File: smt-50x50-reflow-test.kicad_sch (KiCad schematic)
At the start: 0 parts

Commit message: schem: import esp32-c6, uart, usb-c, flash, crystal, buttons, tmp117, bmp581 from esp32c6-sensor-devboard
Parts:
- added AE1: Antenna, RF_Antenna:Johanson_2450AT18x100, symbol Device:Antenna
- added C10, C11, C16, C17, C18, C48, C49, C50, C51: 0u1, Capacitor_SMD:C_0402_1005Metric, symbol Device:C
- added C13: 10n, Capacitor_SMD:C_0402_1005Metric, symbol Device:C
- added C14, C15, C19, C9: 1u, Capacitor_SMD:C_0402_1005Metric, symbol Device:C
- added C20, C8: 10u, Capacitor_SMD:C_0402_1005Metric, symbol Device:C
- added C23, C25: 12p, Capacitor_SMD:C_0402_1005Metric, symbol Device:C
- added C28, C29: 1p2, Capacitor_SMD:C_0402_1005Metric, symbol Device:C
- added C52: 1p, Capacitor_SMD:C_0402_1005Metric, symbol Device:C
- added D7: D_Schottky, Diode_SMD:D_SMA, symbol Device:D_Schottky
- added J1, J8: Conn_01x04_Pin, Connector_PinHeader_2.54mm:PinHeader_1x04_P2.54mm_Vertical, symbol Connector:Conn_01x04_Pin
- added J4: USB_C_Receptacle_USB2.0_14P, Connector_USB:USB_C_Receptacle_HRO_TYPE-C-31-M-12, symbol Connector:USB_C_Receptacle_USB2.0_14P
- added J9: Conn_01x03_Pin, Connector_PinHeader_2.54mm:PinHeader_1x03_P2.54mm_Vertical, symbol Connector:Conn_01x03_Pin
- added L2, L4, L7: 2n7, Inductor_SMD:L_0402_1005Metric, symbol Device:L
- added L3: 24n, Inductor_SMD:L_0402_1005Metric, symbol Device:L
- added L6: 3n9, Inductor_SMD:L_0402_1005Metric, symbol Device:L
- added R1, R2, R3, R4, R5, R6: 0, Resistor_SMD:R_0402_1005Metric, symbol Device:R
- added R10, R14: 22, Resistor_SMD:R_0402_1005Metric, symbol Device:R
- added R12, R13: 5k1, Resistor_SMD:R_0603_1608Metric, symbol Device:R
- added R16: 470, Resistor_SMD:R_0402_1005Metric, symbol Device:R
- added R57, R58, R62, R9: 10k, Resistor_SMD:R_0603_1608Metric, symbol Device:R
- added R7, R8: 10k, symbol Device:R
- added SW1, SW2: SW_Push, Button_Switch_SMD:SW_SPST_TS-1088-xR020, symbol Switch:SW_Push
- added U1: ESP32-C6, Package_DFN_QFN:QFN-40-1EP_5x5mm_P0.4mm_EP3.6x3.6mm_ThermalVias, symbol PCM_Espressif:ESP32-C6
- added U14, U16: TMP117AIDRV, Package_SON:WSON-6-1EP_2x2mm_P0.65mm_EP1x1.6mm, symbol Sensor_Temperature:TMP117xxDRV
- added U15: BMP581, Pers:Bosch_LGA-10_2x2mm_P0.8mm_AntiClockwisePinNumbering, symbol Pers:BMP581
- added U2: W25Q128JVS, Package_SO:SOIC-8_5.3x5.3mm_P1.27mm, symbol Memory_Flash:W25Q128JVS
- added U7: USBLC6-2SC6, Package_TO_SOT_SMD:SOT-23-6, symbol Power_Protection:USBLC6-2SC6
- added Y1: 48M, Crystal:Crystal_SMD_2016-4Pin_2.0x1.6mm, symbol Device:Crystal_GND24
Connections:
- new net: J4.A5 (CC1), R12.2
- new net: J4.A6 (D+), J4.B6 (D+), U7.3 (I/O2)
- new net: J4.A7 (D-), J4.B7 (D-), U7.1 (I/O1)
- new net: J4.B5 (CC2), R13.2
- new net: R2.1, U2.2 (DO/IO_{1})
- new net: R2.2, U1.21 (SPIQ/GPIO25)
- new net: C52.2, L6.2, L7.2
- new net: R5.1, U2.6 (CLK)
- new net: R5.2, U1.25 (SPICLK/GPIO29)
- new net: R58.1, U15.5 (SDO)
- new net: C11.1, L2.2, U1.2 (VDDA3P3), U1.3 (VDDA3P3)
- new net: R1.1, U2.1 (~{CS})
- new net: R3.1, U2.3 (~{WP}/IO_{2})
- new net: R6.1, U2.5 (DI/IO_{0})
- new net: R4.1, U2.7 (~{HOLD}/~{RESET}/IO_{3})
- new net: C15.1, C16.1, U1.23 (VDD_SPI/GPIO27), U2.8 (VCC)
- new net: R1.2, U1.20 (SPICS0/GPIO24)
- new net: J8.1 (Pin_1), U1.10 (MTMS/GPIO4/FSPIHD/ADC1_CH4)
- new net: J8.2 (Pin_2), U1.11 (MTDI/GPIO5/FSPIWP/ADC1_CH5)
- new net: J8.3 (Pin_3), U1.12 (MTCK/GPIO6/FSPICLK/ADC1_CH6)
- new net: J8.4 (Pin_4), U1.13 (MTDO/GPIO7/FSPID)
- new net: R4.2, U1.24 (SPIHD/GPIO28)
- new net: R3.2, U1.22 (SPIWP/GPIO26)
- new net: R6.2, U1.26 (SPID/GPIO30)
- new net: J1.4 (Pin_4), R16.1
- new net: R8.2, U1.15 (GPIO9)
- new net: R7.2, U1.14 (GPIO8)
- new net +3V3: C10.1, C13.1, C14.1, C17.1, C18.1, C48.1, C49.2, C50.1, C51.1, C8.1, C9.1, J1.1 (Pin_1), L2.1, R57.1, R58.2, R62.1, R7.1, R8.1, R9.2, U1.28 (VDDPST2), U1.37 (VDDA1), U1.40 (VDDA2), U1.5 (VDDPST1), U14.5 (V+), U15.1 (VDDIO), U15.10 (VDD), U15.6 (CSB), U16.4 (ADD0), U16.5 (V+)
- new net +5V: C20.1, D7.1 (K)
- new net BMP_INT1: U15.7 (INT)
- new net BOOT/SCL: SW1.2, U14.1 (SCL), U15.2 (SCK), U16.1 (SCL)
- new net CHIP_PU: C19.1, R9.1, SW2.2, U1.4 (CHIP_PU)
- new net D+: R10.2, U7.4 (I/O2)
- new net D-: R14.2, U7.6 (I/O1)
- new net ESP_D+: R10.1, U1.19 (GPIO13/USB_D+)
- new net ESP_D-: R14.1, U1.18 (GPIO12/USB_D-)
- new net GND: C10.2, C11.2, C13.2, C14.2, C15.2, C16.2, C17.2, C18.2, C19.2, C20.2, C23.1, C25.2, C28.2, C29.2, C48.2, C49.1, C50.2, C51.2, C8.2, C9.2, J1.3 (Pin_3), J4.A1 (GND), J4.A12 (GND), J4.B1 (GND), J4.B12 (GND), J4.S1 (SHIELD), J9.1 (Pin_1), J9.2 (Pin_2), J9.3 (Pin_3), L7.1, R12.1, R13.1, SW1.1, SW2.1, U1.41 (GND), U14.2 (GND), U14.4 (ADD0), U15.3 (GND), U15.8 (GND), U15.9 (GND), U16.2 (GND), U2.4 (GND), U7.2 (GND), Y1.2, Y1.4
- new net RF_ANT: AE1.1 (A), L6.1
- new net RF_ESP: C28.1, L4.2, U1.1 (ANT)
- new net RF_TRANS: C29.1, C52.1, L4.1
- new net SDA: U14.6 (SDA), U15.4 (SDI), U16.6 (SDA)
- new net TMP117_ALERT: R57.2, U14.3 (ALERT)
- new net TMP117_ALERT2: R62.2, U16.3 (ALERT)
- new net U0RXD: J1.2 (Pin_2), U1.30 (U0RXD/GPIO17/FSPICS1)
- new net U0TXD: R16.2, U1.29 (U0TXD/GPIO16/FSPICS0)
- new net VBUS: D7.2 (A), J4.A4 (VBUS), J4.A9 (VBUS), J4.B4 (VBUS), J4.B9 (VBUS), U7.5 (VBUS)
- new net XTAL_32K_N: U1.7 (GPIO1/XTAL_32K_N/ADC1_CH1)
- new net XTAL_32K_P: U1.6 (GPIO0/XTAL_32K_P/ADC1_CH0)
- new net XTAL_N: C25.1, U1.38 (XTAL_N), Y1.3
- new net XTAL_P: L3.1, U1.39 (XTAL_P)
- new net XTAL_PL: C23.2, L3.2, Y1.1
- no-connect marks 0 -> 3
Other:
- note added: "BMP581 I2C"
- note added: "Buttons"
- note added: "EN RC delay"
- note added: "HSE"
- note added: "Power"
- note added: "QFlash"
- note added: "TMP117 Temperature 1"
- note added: "TMP117 Temperature 2"
- note added: "UART"
- note added: "USB/ESP"

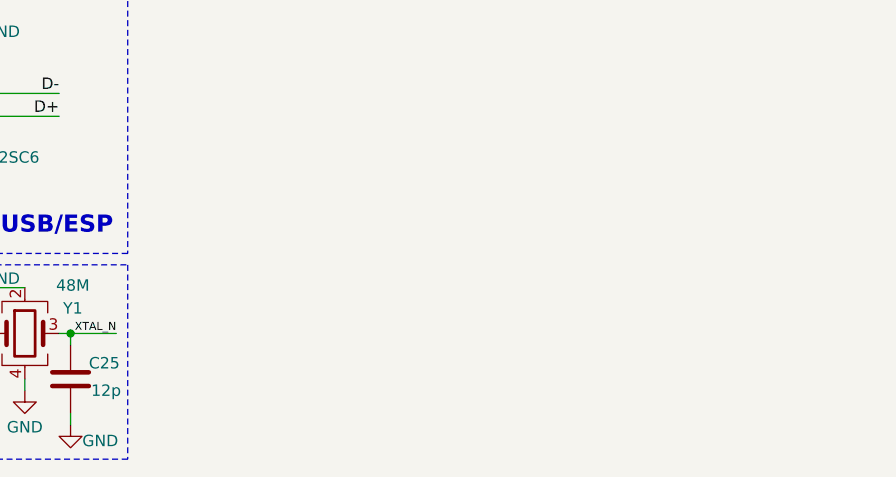
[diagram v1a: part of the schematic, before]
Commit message: schem: add LM317A 3v3 ldo
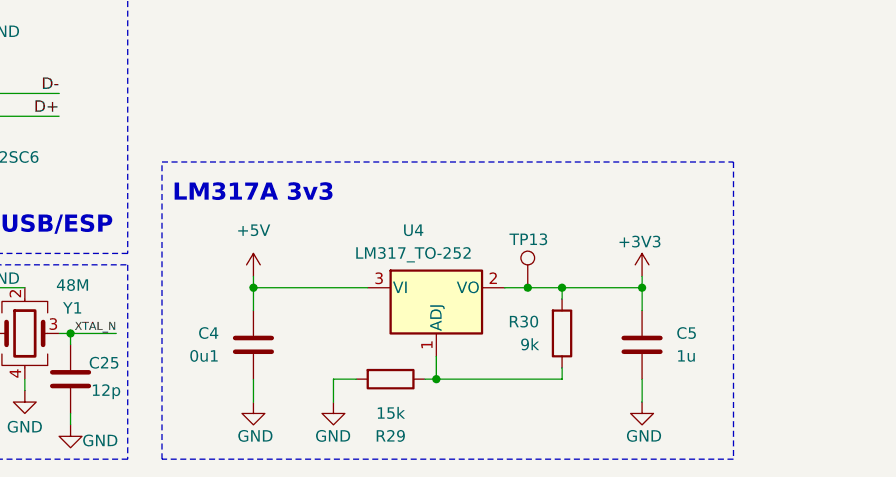
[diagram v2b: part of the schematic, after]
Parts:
- added C4: 0u1, Capacitor_SMD:C_0603_1608Metric, symbol Device:C
- added C5: 1u, Capacitor_SMD:C_0603_1608Metric, symbol Device:C
- added R29: 15k, Resistor_SMD:R_0603_1608Metric, symbol Device:R
- added R30: 9k, Resistor_SMD:R_0603_1608Metric, symbol Device:R
- added TP13: TestPoint, TestPoint:TestPoint_Pad_D2.0mm, symbol Connector:TestPoint
- added U4: LM317_TO-252, Package_TO_SOT_SMD:TO-252-2, symbol Regulator_Linear:LM317_TO-252
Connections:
- net +3V3: now also C5.1, R30.2, TP13.1, U4.2 (VO)
- net +5V: now also C4.1, U4.3 (VI)
- net GND: now also C4.2, C5.2, R29.2
- new net: R29.1, R30.1, U4.1 (ADJ)
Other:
- note added: "LM317A 3v3"

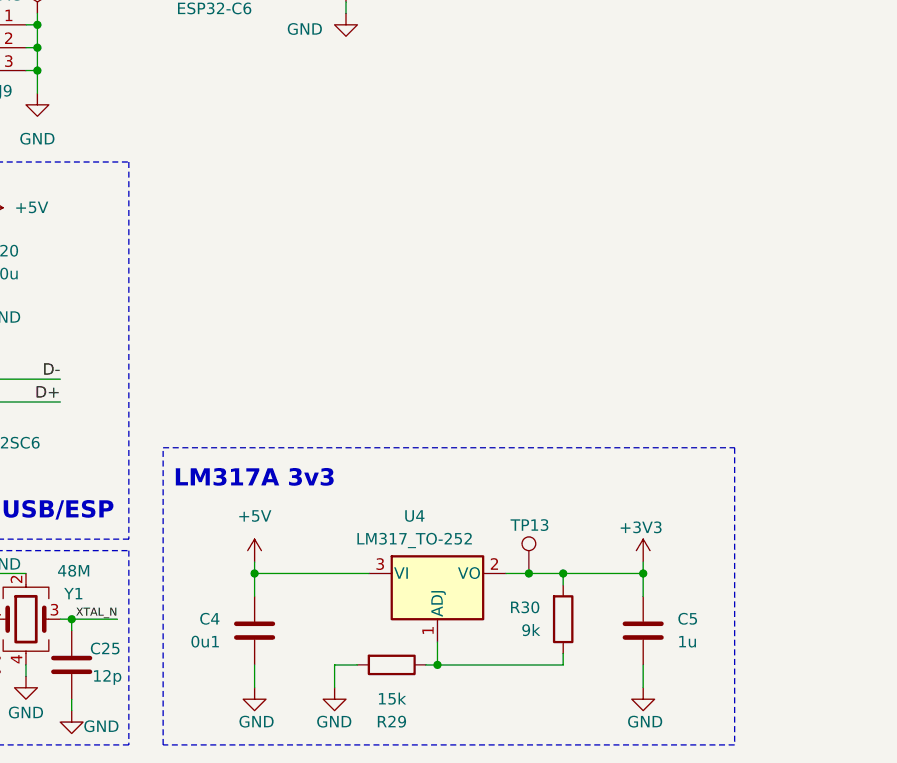
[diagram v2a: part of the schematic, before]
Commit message: schem: import AP2112K 3.3v ldo from esp32c6-sensor-devboard
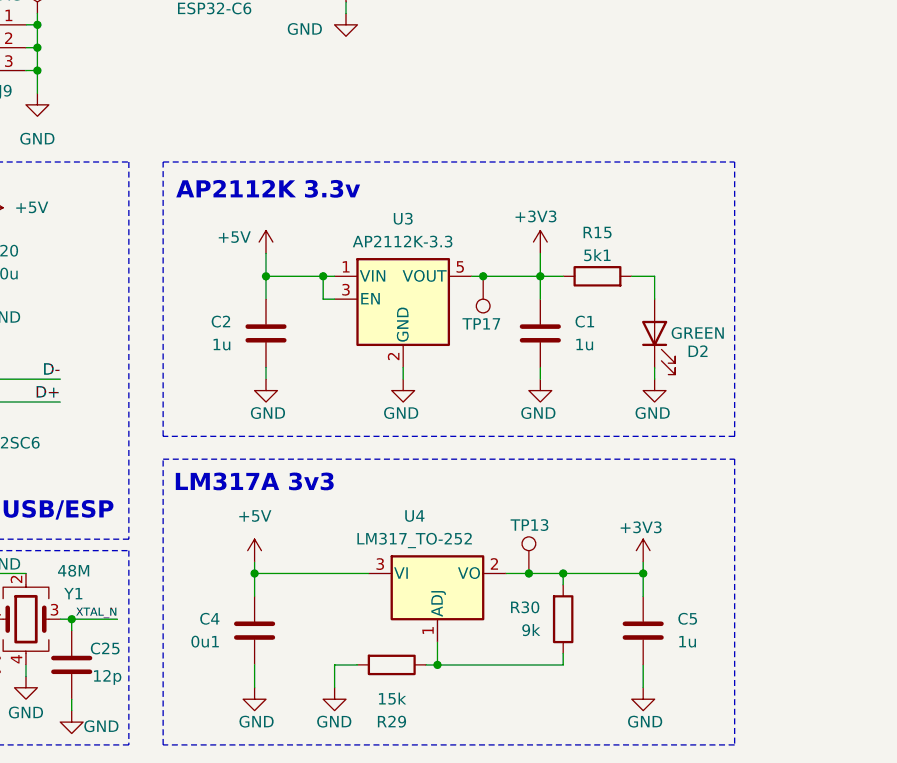
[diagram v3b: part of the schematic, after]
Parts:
- added C1, C2: 1u, Capacitor_SMD:C_0603_1608Metric, symbol Device:C
- added D2: GREEN, LED_SMD:LED_0805_2012Metric, symbol Device:LED
- added R15: 5k1, Resistor_SMD:R_0603_1608Metric, symbol Device:R
- added TP17: TestPoint, TestPoint:TestPoint_Pad_D2.0mm, symbol Connector:TestPoint
- added U3: AP2112K-3.3, Package_TO_SOT_SMD:SOT-23-5, symbol Regulator_Linear:AP2112K-3.3
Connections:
- net +3V3: now also C1.1, R15.1, TP17.1, U3.5 (VOUT)
- net +5V: now also C2.1, U3.1 (VIN), U3.3 (EN)
- net GND: now also C1.2, C2.2, D2.1 (K), U3.2 (GND)
- new net: D2.2 (A), R15.2
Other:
- note added: "AP2112K 3.3v"

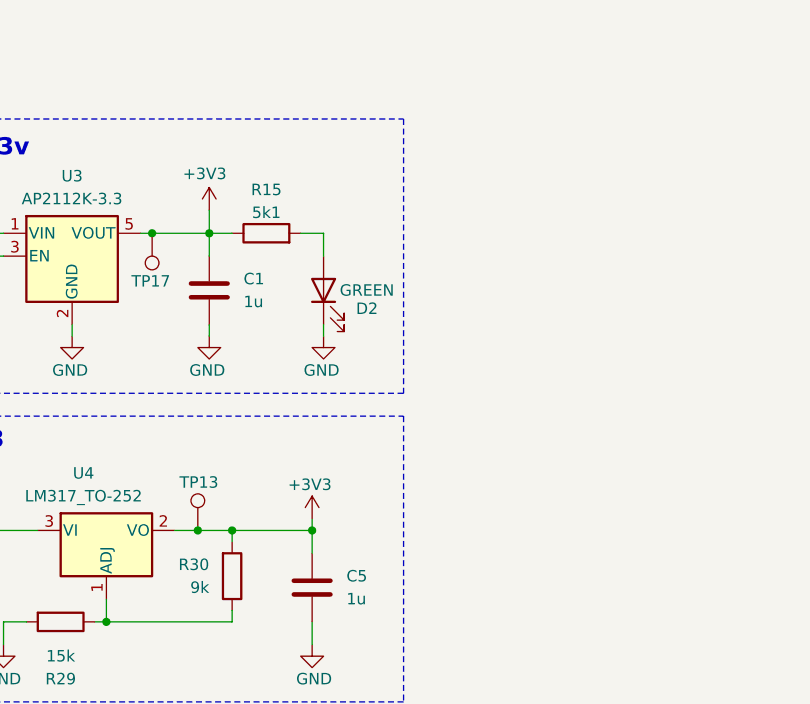
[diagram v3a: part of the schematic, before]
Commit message: schem: import ldo select from esp32s3-poc-devboard
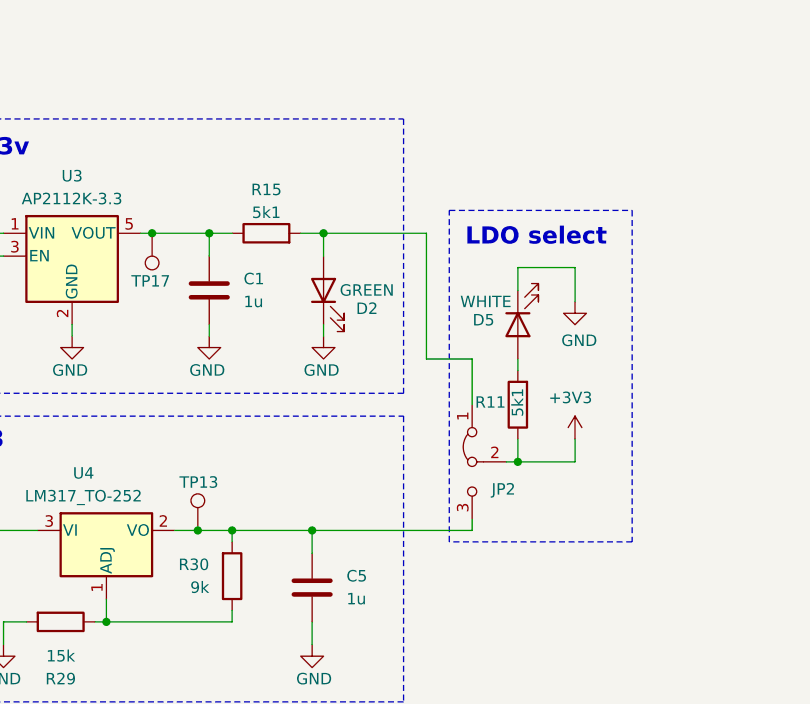
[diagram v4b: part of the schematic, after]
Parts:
- added D5: WHITE, LED_SMD:LED_0603_1608Metric, symbol Device:LED
- added JP2: Jumper_3_Bridged12, Connector_PinHeader_2.54mm:PinHeader_1x03_P2.54mm_Vertical, symbol Jumper:Jumper_3_Bridged12
- added R11: 5k1, Resistor_SMD:R_0603_1608Metric, symbol Device:R
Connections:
- net +3V3: now also JP2.2 (C), R11.1; no longer C1.1, C5.1, R15.1, R30.2, TP13.1, TP17.1, U3.5 (VOUT), U4.2 (VO)
- net GND: now also D5.1 (K)
- net at D2.2 (A), R15.2: now also JP2.1 (A)
- new net: C5.1, JP2.3 (B), R30.2, TP13.1, U4.2 (VO)
- new net: D5.2 (A), R11.2
- new net: C1.1, R15.1, TP17.1, U3.5 (VOUT)
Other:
- note added: "LDO select"
